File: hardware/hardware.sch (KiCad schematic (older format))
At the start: 2 parts

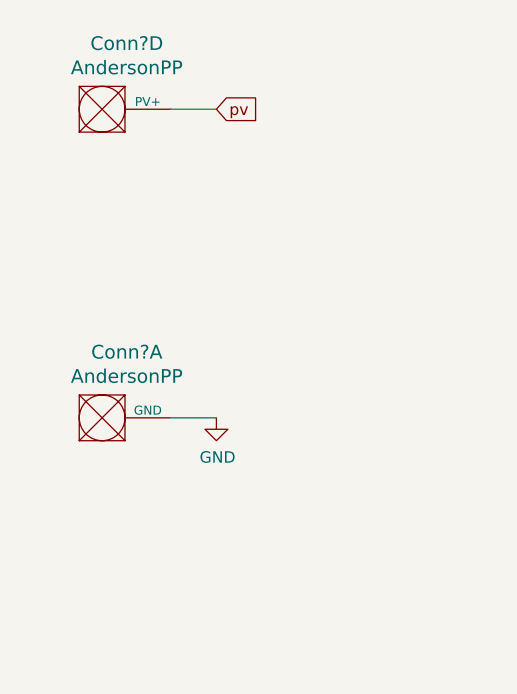
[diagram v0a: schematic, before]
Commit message: Added Placeholders
Added Capacitor bank placeholder and Thermistor measurement placeholder.
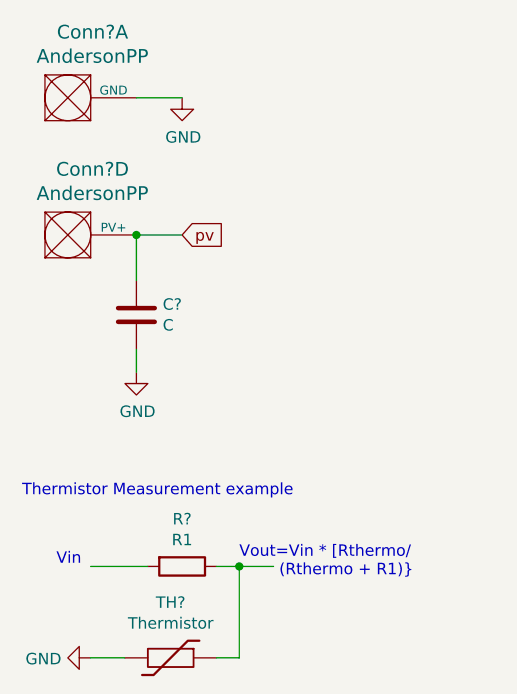
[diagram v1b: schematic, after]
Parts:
- added C?: C, symbol Device:C
- added R?: R1, symbol Device:R
- added TH?: Thermistor, symbol Device:Thermistor
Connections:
- wire segments 2 -> 10
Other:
- note added: "Thermistor Measurement example"
- note added: "Vin"
- note added: "Vout=Vin * [Rthermo/\n (Rthermo + R1)}"
- moved on the sheet: Conn?A, Conn?D
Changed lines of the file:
@@
 L MRDT_Connectors:AndersonPP Conn?
 U 4 1 614D2045
-P 850 1050
-F 0 "Conn?" H 1058 1437 60  0000 C CNN
-F 1 "AndersonPP" H 1058 1331 60  0000 C CNN
-F 2 "" H 700 500 60  0001 C CNN
-F 3 "" H 700 500 60  0001 C CNN
-	4    850  1050
+P 700 1600
+F 0 "Conn?" H 908 1987 60  0000 C CNN
+F 1 "AndersonPP" H 908 1881 60  0000 C CNN
+F 2 "" H 550 1050 60  0001 C CNN
+F 3 "" H 550 1050 60  0001 C CNN
+	4    700  1600
 	1    0    0    -1
 $EndComp
@@
 L MRDT_Connectors:AndersonPP Conn?
 U 1 1 614D689F
-P 850 2400
-F 0 "Conn?" H 1058 2787 60  0000 C CNN
-F 1 "AndersonPP" H 1058 2681 60  0000 C CNN
-F 2 "" H 700 1850 60  0001 C CNN
-F 3 "" H 700 1850 60  0001 C CNN
-	1    850  2400
+P 700 1000
+F 0 "Conn?" H 908 1387 60  0000 C CNN
+F 1 "AndersonPP" H 908 1281 60  0000 C CNN
+F 2 "" H 550 450 60  0001 C CNN
+F 3 "" H 550 450 60  0001 C CNN
+	1    700  1000
 	1    0    0    -1
 $EndComp
@@
 L power:GND #PWR?
 U 1 1 614D71DD
-P 1450 2300
-F 0 "#PWR?" H 1450 2050 50  0001 C CNN
-F 1 "GND" H 1455 2127 50  0000 C CNN
-F 2 "" H 1450 2300 50  0001 C CNN
-F 3 "" H 1450 2300 50  0001 C CNN
-	1    1450 2300
+P 1300 900
+F 0 "#PWR?" H 1300 650 50  0001 C CNN
+F 1 "GND" H 1305 727 50  0000 C CNN
+F 2 "" H 1300 900 50  0001 C CNN
+F 3 "" H 1300 900 50  0001 C CNN
+	1    1300 900
 	1    0    0    -1
 $EndComp
 Wire Wire Line
-	1450 2300 1250 2300
-Text GLabel 1450 950  2    50   Input ~ 0
+	1300 900  1100 900
+Text GLabel 1300 1500 2    50   Input ~ 0
 pv
 Wire Wire Line
-	1450 950  1250 950
+	1300 1500 1100 1500
+$Comp
+L Device:C C?
+U 1 1 614D2AA6
+P 1100 1850
+F 0 "C?" H 985 1804 50  0000 R CNN
+F 1 "C" H 985 1895 50  0000 R CNN
+F 2 "" H 1138 1700 50  0001 C CNN
+F 3 "~" H 1100 1850 50  0001 C CNN
+	1    1100 1850
+	-1   0    0    1
+$EndComp
+Wire Wire Line
+	1100 1700 1100 1500
+Connection ~ 1100 1500
+Wire Wire Line
+	1100 2000 1100 2100
+$Comp
+L power:GND #PWR?
+U 1 1 614D4A55
+P 1100 2100
+F 0 "#PWR?" H 1100 1850 50  0001 C CNN
+F 1 "GND" H 1105 1927 50  0000 C CNN
+F 2 "" H 1100 2100 50  0001 C CNN
+F 3 "" H 1100 2100 50  0001 C CNN
+	1    1100 2100
+	1    0    0    -1
+$EndComp
+$Comp
+L Device:R R?
+U 1 1 614D88F5
+P 1300 2950
+F 0 "R?" V 1093 2950 50  0000 C CNN
+F 1 "R1" V 1184 2950 50  0000 C CNN
+F 2 "" V 1230 2950 50  0001 C CNN
+F 3 "~" H 1300 2950 50  0001 C CNN
+	1    1300 2950
+	0    1    1    0
+$EndComp
+Wire Wire Line
+	1550 3350 1450 3350
+$Comp
+L Device:Thermistor TH?
+U 1 1 614D97E1
+P 1250 3350
+F 0 "TH?" V 1008 3350 50  0000 C CNN
+F 1 "Thermistor" V 1099 3350 50  0000 C CNN
+F 2 "" H 1250 3350 50  0001 C CNN
+F 3 "~" H 1250 3350 50  0001 C CNN
+	1    1250 3350
+	0    1    1    0
+$EndComp
+Wire Wire Line
+	900  3350 1050 3350
+Wire Wire Line
+	900  2950 1150 2950
+$Comp
+L power:GND #PWR?
+U 1 1 614DAA27
+P 900 3350
+F 0 "#PWR?" H 900 3100 50  0001 C CNN
+F 1 "GND" V 905 3222 50  0000 R CNN
+F 2 "" H 900 3350 50  0001 C CNN
+F 3 "" H 900 3350 50  0001 C CNN
+	1    900  3350
+	0    1    1    0
+$EndComp
+Text Notes 750  2950 0    50   ~ 0
+Vin
+Wire Wire Line
+	1450 2950 1550 2950
+Wire Wire Line
+	1550 2950 1550 3350
+Connection ~ 1550 2950
+Wire Wire Line
+	1550 2950 1700 2950
+Text Notes 1550 3000 0    50   ~ 0
+Vout=Vin * [Rthermo/\n        (Rthermo + R1)}
+Text Notes 600  2650 0    50   ~ 0
+Thermistor Measurement example
 $EndSCHEMATC

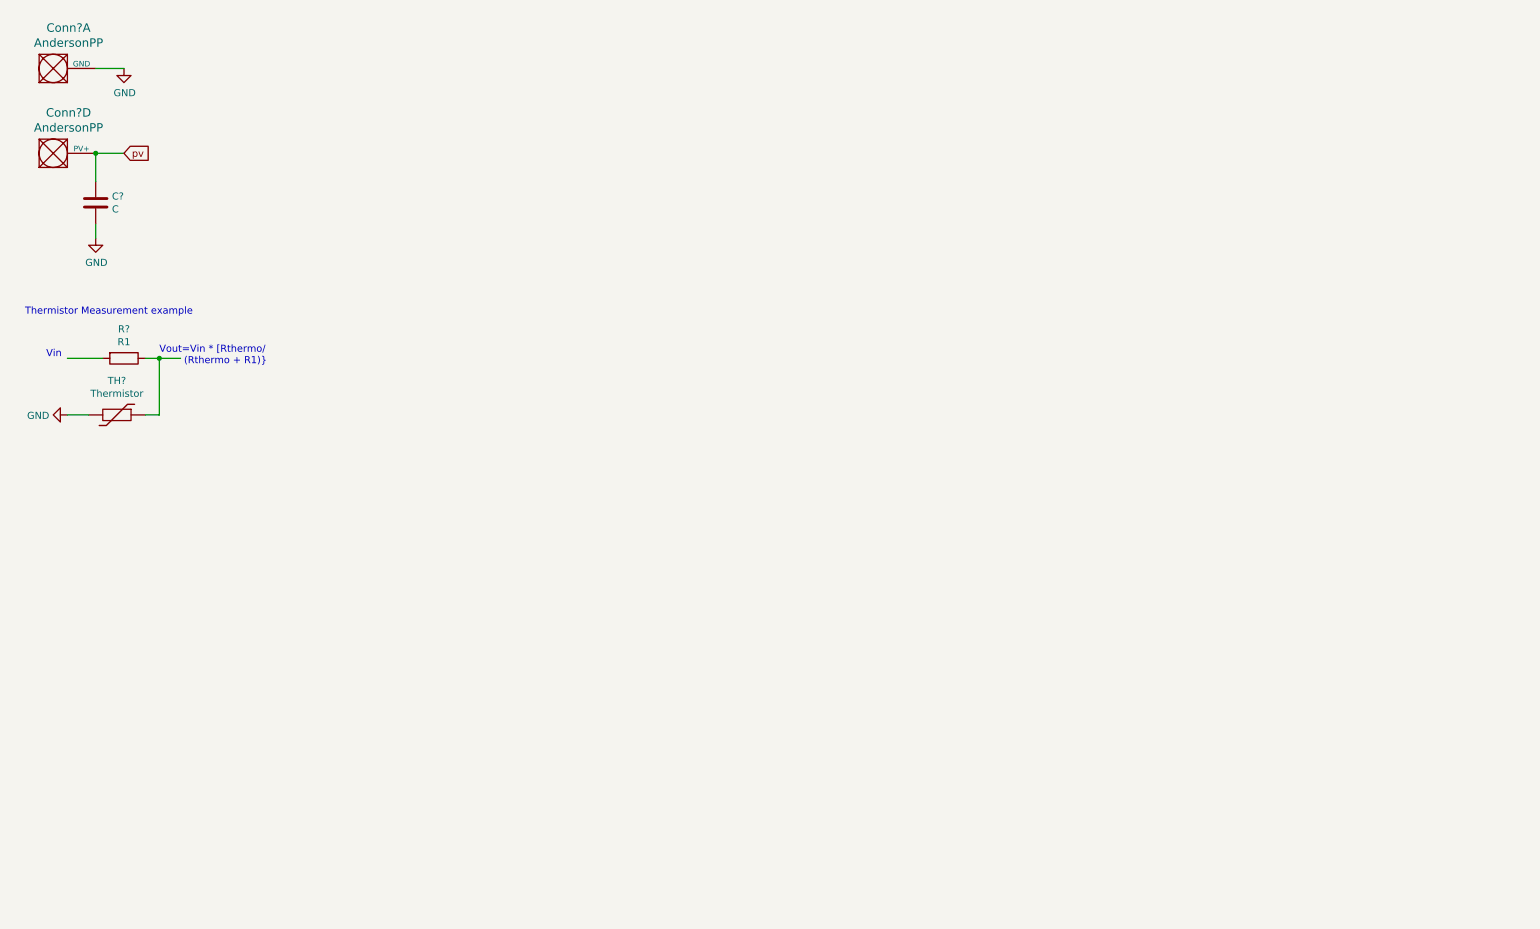
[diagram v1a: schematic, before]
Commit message: Worked on mosfet driver
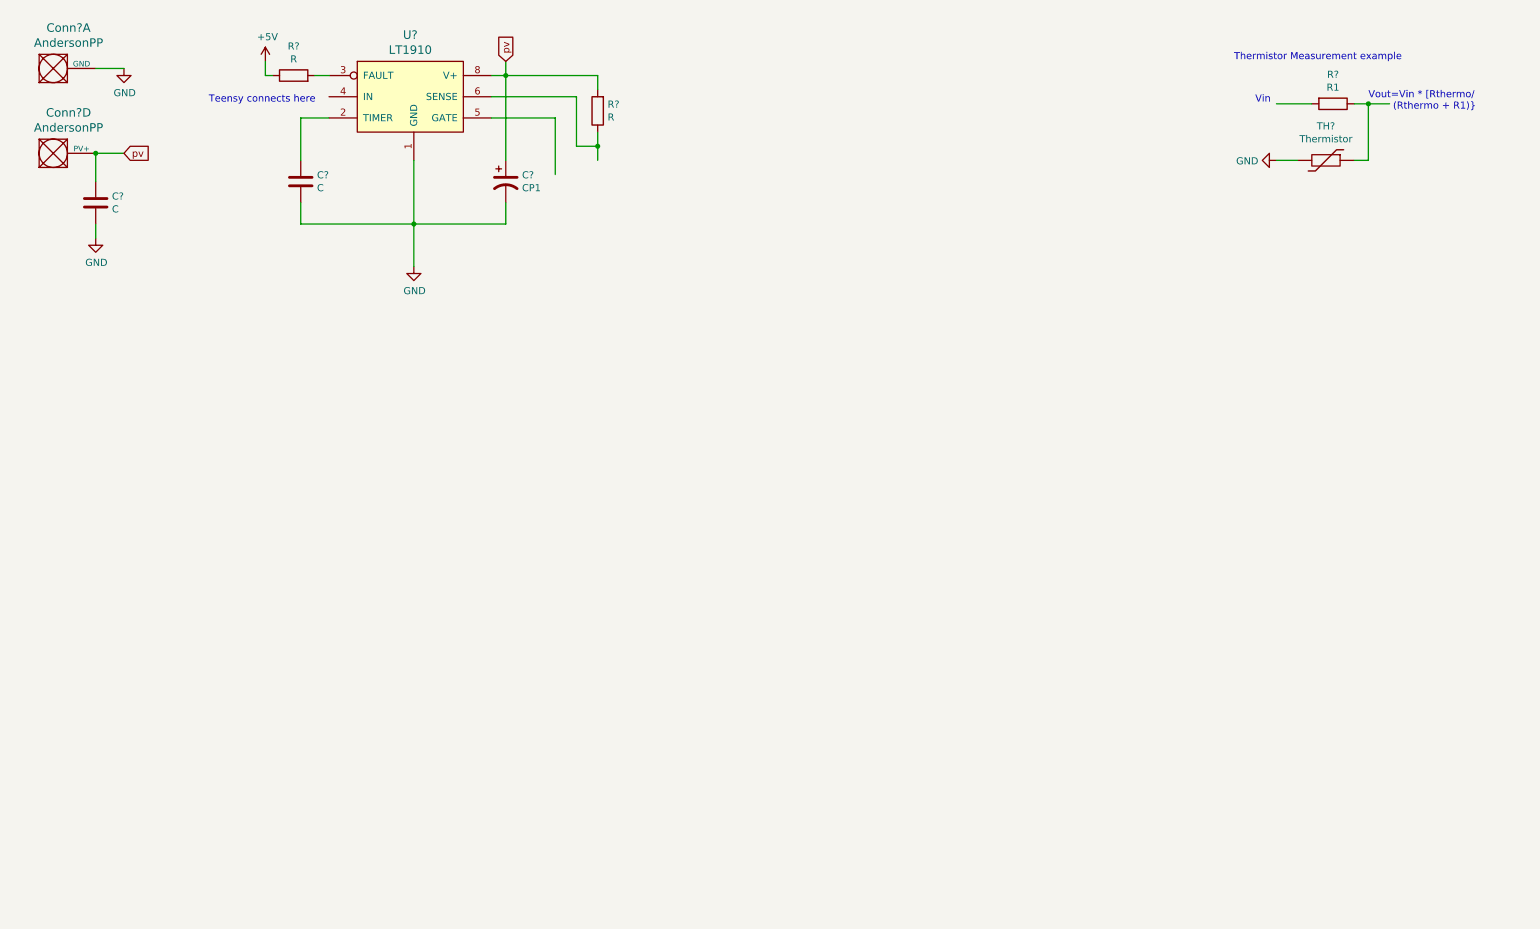
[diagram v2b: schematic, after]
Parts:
- added C?: C, symbol Device:C
- added C?: CP1, symbol Device:CP1
- added R? (x2): R, symbol Device:R
- added U?: LT1910, symbol MRDT_ICs:LT1910
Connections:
- net labels added: +5V
- wire segments 10 -> 33
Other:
- note added: "Teensy connects here"
- moved on the sheet: R?, TH?
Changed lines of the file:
@@
 L Device:R R?
 U 1 1 614D88F5
-P 1300 2950
-F 0 "R?" V 1093 2950 50  0000 C CNN
-F 1 "R1" V 1184 2950 50  0000 C CNN
-F 2 "" V 1230 2950 50  0001 C CNN
-F 3 "~" H 1300 2950 50  0001 C CNN
-	1    1300 2950
+P 9850 1150
+F 0 "R?" V 9643 1150 50  0000 C CNN
+F 1 "R1" V 9734 1150 50  0000 C CNN
+F 2 "" V 9780 1150 50  0001 C CNN
+F 3 "~" H 9850 1150 50  0001 C CNN
+	1    9850 1150
 	0    1    1    0
 $EndComp
 Wire Wire Line
-	1550 3350 1450 3350
+	10100 1550 10000 1550
 $Comp
 L Device:Thermistor TH?
 U 1 1 614D97E1
-P 1250 3350
-F 0 "TH?" V 1008 3350 50  0000 C CNN
-F 1 "Thermistor" V 1099 3350 50  0000 C CNN
-F 2 "" H 1250 3350 50  0001 C CNN
-F 3 "~" H 1250 3350 50  0001 C CNN
-	1    1250 3350
+P 9800 1550
+F 0 "TH?" V 9558 1550 50  0000 C CNN
+F 1 "Thermistor" V 9649 1550 50  0000 C CNN
+F 2 "" H 9800 1550 50  0001 C CNN
+F 3 "~" H 9800 1550 50  0001 C CNN
+	1    9800 1550
 	0    1    1    0
 $EndComp
 Wire Wire Line
-	900  3350 1050 3350
+	9450 1550 9600 1550
 Wire Wire Line
-	900  2950 1150 2950
+	9450 1150 9700 1150
 $Comp
 L power:GND #PWR?
 U 1 1 614DAA27
-P 900 3350
-F 0 "#PWR?" H 900 3100 50  0001 C CNN
-F 1 "GND" V 905 3222 50  0000 R CNN
-F 2 "" H 900 3350 50  0001 C CNN
-F 3 "" H 900 3350 50  0001 C CNN
-	1    900  3350
+P 9450 1550
+F 0 "#PWR?" H 9450 1300 50  0001 C CNN
+F 1 "GND" V 9455 1422 50  0000 R CNN
+F 2 "" H 9450 1550 50  0001 C CNN
+F 3 "" H 9450 1550 50  0001 C CNN
+	1    9450 1550
 	0    1    1    0
 $EndComp
-Text Notes 750  2950 0    50   ~ 0
+Text Notes 9300 1150 0    50   ~ 0
 Vin
 Wire Wire Line
-	1450 2950 1550 2950
+	10000 1150 10100 1150
 Wire Wire Line
-	1550 2950 1550 3350
-Connection ~ 1550 2950
+	10100 1150 10100 1550
+Connection ~ 10100 1150
 Wire Wire Line
-	1550 2950 1700 2950
-Text Notes 1550 3000 0    50   ~ 0
+	10100 1150 10250 1150
+Text Notes 10100 1200 0    50   ~ 0
 Vout=Vin * [Rthermo/\n        (Rthermo + R1)}
-Text Notes 600  2650 0    50   ~ 0
+Text Notes 9150 850  0    50   ~ 0
 Thermistor Measurement example
+$Comp
+L MRDT_ICs:LT1910 U?
+U 1 1 61539417
+P 2950 1350
+F 0 "U?" H 3325 2037 60  0000 C CNN
+F 1 "LT1910" H 3325 1931 60  0000 C CNN
+F 2 "" H 2950 1350 60  0001 C CNN
+F 3 "" H 2950 1350 60  0001 C CNN
+	1    2950 1350
+	1    0    0    -1
+$EndComp
+$Comp
+L power:+5V #PWR?
+U 1 1 6153AF38
+P 2300 850
+F 0 "#PWR?" H 2300 700 50  0001 C CNN
+F 1 "+5V" H 2315 1023 50  0000 C CNN
+F 2 "" H 2300 850 50  0001 C CNN
+F 3 "" H 2300 850 50  0001 C CNN
+	1    2300 850
+	1    0    0    -1
+$EndComp
+Wire Wire Line
+	4000 850  4000 950
+Wire Wire Line
+	4000 950  3900 950
+$Comp
+L power:GND #PWR?
+U 1 1 6153BB70
+P 3350 2300
+F 0 "#PWR?" H 3350 2050 50  0001 C CNN
+F 1 "GND" H 3355 2127 50  0000 C CNN
+F 2 "" H 3350 2300 50  0001 C CNN
+F 3 "" H 3350 2300 50  0001 C CNN
+	1    3350 2300
+	1    0    0    -1
+$EndComp
+Wire Wire Line
+	3350 2300 3350 2000
+$Comp
+L Device:C C?
+U 1 1 6153D4FA
+P 2550 1700
+F 0 "C?" H 2665 1746 50  0000 L CNN
+F 1 "C" H 2665 1655 50  0000 L CNN
+F 2 "" H 2588 1550 50  0001 C CNN
+F 3 "~" H 2550 1700 50  0001 C CNN
+	1    2550 1700
+	1    0    0    -1
+$EndComp
+Wire Wire Line
+	2750 1250 2550 1250
+Wire Wire Line
+	2550 1250 2550 1550
+$Comp
+L Device:CP1 C?
+U 1 1 6153E02C
+P 4000 1700
+F 0 "C?" H 4115 1746 50  0000 L CNN
+F 1 "CP1" H 4115 1655 50  0000 L CNN
+F 2 "" H 4000 1700 50  0001 C CNN
+F 3 "~" H 4000 1700 50  0001 C CNN
+	1    4000 1700
+	1    0    0    -1
+$EndComp
+Wire Wire Line
+	4000 1550 4000 950
+Connection ~ 4000 950
+Wire Wire Line
+	2550 1850 2550 2000
+Wire Wire Line
+	2550 2000 3350 2000
+Wire Wire Line
+	4000 2000 4000 1850
+Connection ~ 3350 2000
+Wire Wire Line
+	3350 2000 3350 1550
+Wire Wire Line
+	3350 2000 4000 2000
+$Comp
+L Device:R R?
+U 1 1 6153F28E
+P 4650 1200
+F 0 "R?" H 4580 1154 50  0000 R CNN
+F 1 "R" H 4580 1245 50  0000 R CNN
+F 2 "" V 4580 1200 50  0001 C CNN
+F 3 "~" H 4650 1200 50  0001 C CNN
+	1    4650 1200
+	-1   0    0    1
+$EndComp
+Wire Wire Line
+	4650 1050 4650 950
+Wire Wire Line
+	4650 950  4000 950
+Text GLabel 4000 850  1    50   Input ~ 0
+pv
+$Comp
+L Device:R R?
+U 1 1 61541666
+P 2500 950
+F 0 "R?" V 2707 950 50  0000 C CNN
+F 1 "R" V 2616 950 50  0000 C CNN
+F 2 "" V 2430 950 50  0001 C CNN
+F 3 "~" H 2500 950 50  0001 C CNN
+	1    2500 950
+	0    -1   -1   0
+$EndComp
+Wire Wire Line
+	2300 850  2300 950
+Wire Wire Line
+	2300 950  2350 950
+Wire Wire Line
+	2650 950  2750 950
+Text Notes 1900 1150 0    50   ~ 0
+Teensy connects here
+Wire Wire Line
+	3900 1100 4500 1100
+Wire Wire Line
+	4500 1100 4500 1450
+Wire Wire Line
+	4500 1450 4650 1450
+Wire Wire Line
+	4650 1450 4650 1350
+Wire Wire Line
+	4650 1450 4650 1550
+Connection ~ 4650 1450
+Wire Wire Line
+	3900 1250 4350 1250
+Wire Wire Line
+	4350 1250 4350 1650
 $EndSCHEMATC

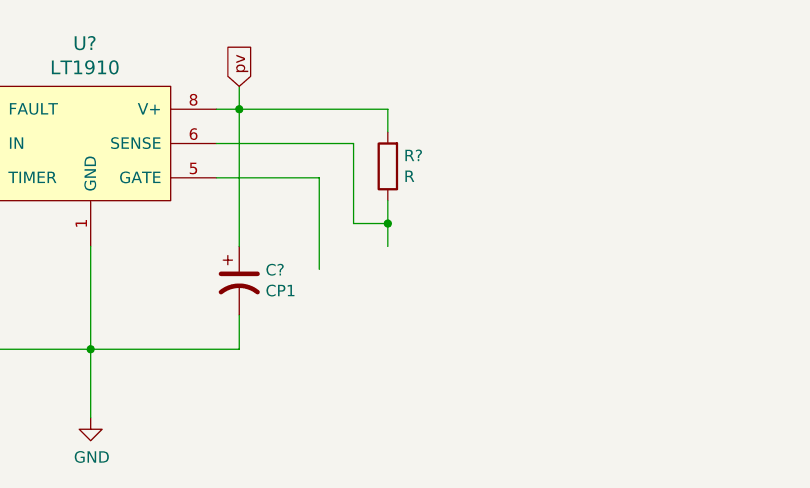
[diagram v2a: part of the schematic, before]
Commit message: Worked on mosfet driver
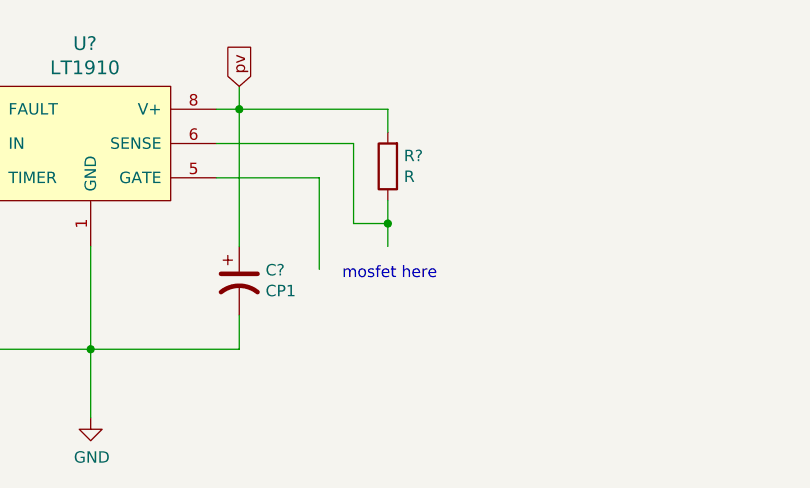
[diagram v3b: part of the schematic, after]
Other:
- note added: "mosfet here"
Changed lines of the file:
@@
 Wire Wire Line
 	4350 1250 4350 1650
+Text Notes 4450 1700 0    50   ~ 0
+mosfet here
 $EndSCHEMATC

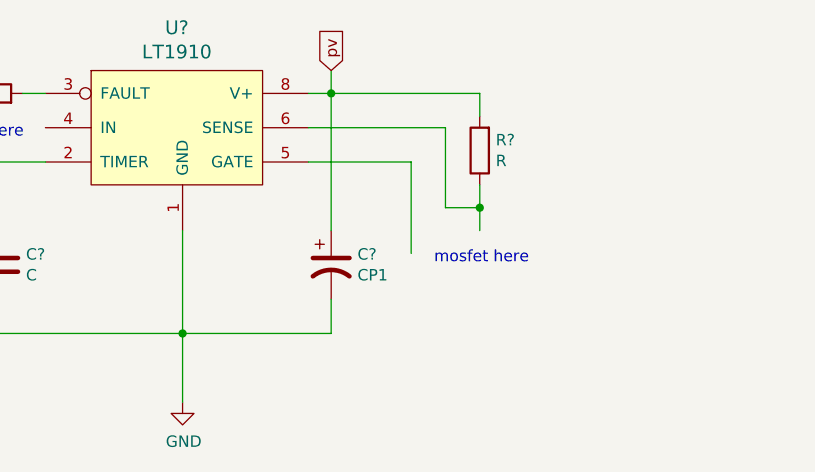
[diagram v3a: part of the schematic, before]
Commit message: Added mosfet
Went with BUK7M33-60EX with 60V and 24A. May need to switch this out with a different amperage
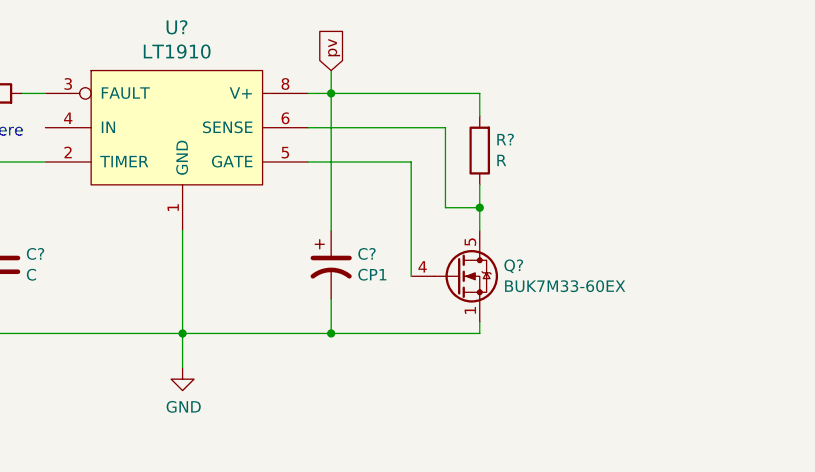
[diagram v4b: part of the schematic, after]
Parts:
- added Q?: BUK7M33-60EX, Package_TO_SOT_SMD:LFPAK33, symbol Transistor_FET:BUK7M33-60EX
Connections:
- wire segments 33 -> 35
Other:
- note removed: "mosfet here"
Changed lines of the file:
@@
 	4000 950  3900 950
-$Comp
-L power:GND #PWR?
-U 1 1 6153BB70
-P 3350 2300
-F 0 "#PWR?" H 3350 2050 50  0001 C CNN
-F 1 "GND" H 3355 2127 50  0000 C CNN
-F 2 "" H 3350 2300 50  0001 C CNN
-F 3 "" H 3350 2300 50  0001 C CNN
-	1    3350 2300
-	1    0    0    -1
-$EndComp
-Wire Wire Line
-	3350 2300 3350 2000
 $Comp
 L Device:C C?
@@
 Wire Wire Line
 	4650 1450 4650 1350
-Wire Wire Line
-	4650 1450 4650 1550
 Connection ~ 4650 1450
 Wire Wire Line
 	3900 1250 4350 1250
 Wire Wire Line
-	4350 1250 4350 1650
-Text Notes 4450 1700 0    50   ~ 0
-mosfet here
+	4650 1450 4650 1550
+Wire Wire Line
+	4350 1250 4350 1750
+$Comp
+L Transistor_FET:BUK7M33-60EX Q?
+U 1 1 6158AC0E
+P 4550 1750
+F 0 "Q?" H 4754 1796 50  0000 L CNN
+F 1 "BUK7M33-60EX" H 4754 1705 50  0000 L CNN
+F 2 "Package_TO_SOT_SMD:LFPAK33" H 4750 1675 50  0001 L CIN
+F 3 "https://assets.nexperia.com/documents/data-sheet/BUK7M33-60E.pdf" V 4550 1750 50  0001 L CNN
+	1    4550 1750
+	1    0    0    -1
+$EndComp
+Wire Wire Line
+	4000 2000 4650 2000
+Wire Wire Line
+	4650 2000 4650 1950
+Connection ~ 4000 2000
+$Comp
+L power:GND #PWR?
+U 1 1 6153BB70
+P 3350 2150
+F 0 "#PWR?" H 3350 1900 50  0001 C CNN
+F 1 "GND" H 3355 1977 50  0000 C CNN
+F 2 "" H 3350 2150 50  0001 C CNN
+F 3 "" H 3350 2150 50  0001 C CNN
+	1    3350 2150
+	1    0    0    -1
+$EndComp
+Wire Wire Line
+	3350 2150 3350 2000
 $EndSCHEMATC
